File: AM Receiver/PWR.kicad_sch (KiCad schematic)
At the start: 10 parts, among them IC105 L78L08_SO8, IC106 L78L05_SO8, J100 Barrel_Jack_Switch

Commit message: Filled out information in User.Drawings on PCB
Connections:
- net +12V ...+15V renamed VIN
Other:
- note added: "Design Notes - Versorgung Eingang über J100: +12V ... +15V gegen GND. IC106 (L78L05) erzeugt +5V für PLL/Digitalteil; IC105 (L78L08) erzeugt +8V für RF/ZF-Analogteil. 78Lxx Regler sind für ca. 100 mA ausgelegt; Strombudget je Schiene darunter halten. Dropout/Verlustleistung: 12V Minimum gibt genuegend Reserve für 5V/8V Linearregler. C125/C130/C133 = 100 nF dienen als lokale Ein-/Ausgangsabblockun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"
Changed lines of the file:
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@@
 		(comment 3 "T. Brown")
+	)
+	(text "Design Notes - Versorgung\nEingang über J100: +12V ... +15V gegen GND.\nIC106 (L78L05) erzeugt +5V für PLL/Digitalteil; IC105 (L78L08) erzeugt +8V für RF/ZF-Analogteil.\n78Lxx Regler sind für ca. 100 mA ausgelegt; Strombudget je Schiene darunter halten.\nDropout/Verlustleistung: 12V Minimum gibt genuegend Reserve für 5V/8V Linearregler.\nC125/C130/C133 = 100 nF dienen als lokale Ein-/Ausgangsabblockung der Regler.\nTP_VIN, TP_5V, TP_8V und TP_GND sind Bring-up Messpunkte.\nTrennung +5V digital und +8V analog reduziert digitale Störung im RF/ZF-Teil."
+		(exclude_from_sim no)
+		(at 35.56 34.29 0)
+		(effects
+			(font
+				(size 1.27 1.27)
+			)
+			(justify left)
+		)
 	)
 	(junction
@@
 			)
 		)
-		(property "Value" "+12V ...+15V"
+		(property "Value" "VIN"
 			(at 107.696 88.9 0)
 			(show_name no)
@@
 			)
 		)
-		(property "Value" "+12V ...+15V"
+		(property "Value" "VIN"
 			(at 167.386 80.518 0)
 			(show_name no)
@@
 			)
 		)
-		(property "Value" "+12V ...+15V"
+		(property "Value" "VIN"
 			(at 214.376 80.518 0)
 			(show_name no)

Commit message: Updated Design notes in schematic
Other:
- note added: "Design Notes - Versorgung Eingang ueber J100: VIN, vorgesehen fuer 12V ... 15V gegen GND. IC106 (L78L05) erzeugt +5V fuer PLL/Digitalteil; IC105 (L78L08) erzeugt +8V fuer RF/ZF-Analogteil. 78Lxx Regler sind fuer ca. 100 mA ausgelegt; Strombudget je Schiene darunter halten. Dropout/Verlustleistung: 12V Minimum gibt genuegend Reserve fuer 5V/8V Linearregler. C125/C130/C133 = 100 nF dienen als lokal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"
- note removed: "Design Notes - Versorgung Eingang über J100: +12V ... +15V gegen GND. IC106 (L78L05) erzeugt +5V für PLL/Digitalteil; IC105 (L78L08) erzeugt +8V für RF/ZF-Analogteil. 78Lxx Regler sind für ca. 100 mA ausgelegt; Strombudget je Schiene darunter halten. Dropout/Verlustleistung: 12V Minimum gibt genuegend Reserve für 5V/8V Linearregler. C125/C130/C133 = 100 nF dienen als lokale Ein-/Ausgangsabblockun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"
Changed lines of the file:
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@@
 		(comment 3 "T. Brown")
 	)
-	(text "Design Notes - Versorgung\nEingang über J100: +12V ... +15V gegen GND.\nIC106 (L78L05) erzeugt +5V für PLL/Digitalteil; IC105 (L78L08) erzeugt +8V für RF/ZF-Analogteil.\n78Lxx Regler sind für ca. 100 mA ausgelegt; Strombudget je Schiene darunter halten.\nDropout/Verlustleistung: 12V Minimum gibt genuegend Reserve für 5V/8V Linearregler.\nC125/C130/C133 = 100 nF dienen als lokale Ein-/Ausgangsabblockung der Regler.\nTP_VIN, TP_5V, TP_8V und TP_GND sind Bring-up Messpunkte.\nTrennung +5V digital und +8V analog reduziert digitale Störung im RF/ZF-Teil."
+	(text "Design Notes - Versorgung\nEingang ueber J100: VIN, vorgesehen fuer 12V ... 15V gegen GND.\nIC106 (L78L05) erzeugt +5V fuer PLL/Digitalteil; IC105 (L78L08) erzeugt +8V fuer RF/ZF-Analogteil.\n78Lxx Regler sind fuer ca. 100 mA ausgelegt; Strombudget je Schiene darunter halten.\nDropout/Verlustleistung: 12V Minimum gibt genuegend Reserve fuer 5V/8V Linearregler.\nC125/C130/C133 = 100 nF dienen als lokale Ein-/Ausgangsabblockung der Regler.\nTP_VIN, TP_5V, TP_8V und TP_GND sind Bring-up Messpunkte.\nTrennung +5V digital und +8V analog reduziert digitale Stoerung im RF/ZF-Teil."
 		(exclude_from_sim no)
 		(at 35.56 34.29 0)

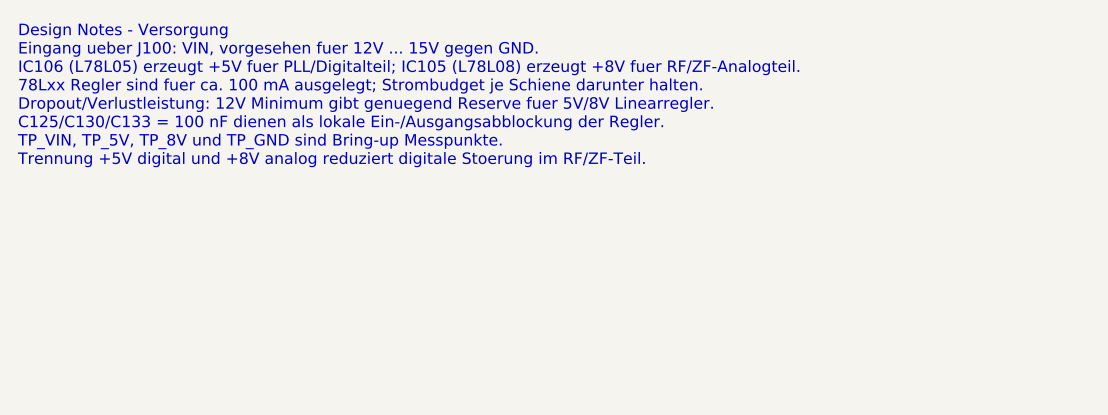
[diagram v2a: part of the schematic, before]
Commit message: updated schematic root page voltage
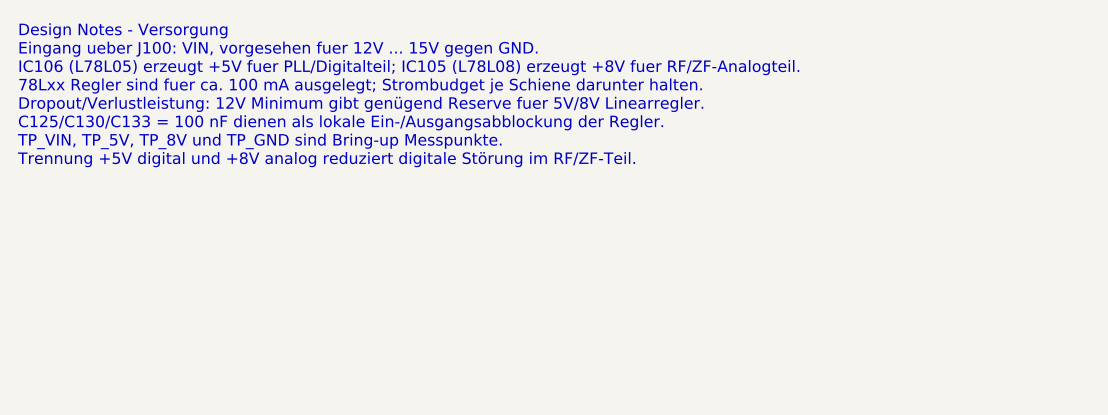
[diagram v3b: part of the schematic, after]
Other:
- note added: "Design Notes - Versorgung Eingang ueber J100: VIN, vorgesehen fuer 12V ... 15V gegen GND. IC106 (L78L05) erzeugt +5V fuer PLL/Digitalteil; IC105 (L78L08) erzeugt +8V fuer RF/ZF-Analogteil. 78Lxx Regler sind fuer ca. 100 mA ausgelegt; Strombudget je Schiene darunter halten. Dropout/Verlustleistung: 12V Minimum gibt genügend Reserve fuer 5V/8V Linearregler. C125/C130/C133 = 100 nF dienen als lokale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"
- note removed: "Design Notes - Versorgung Eingang ueber J100: VIN, vorgesehen fuer 12V ... 15V gegen GND. IC106 (L78L05) erzeugt +5V fuer PLL/Digitalteil; IC105 (L78L08) erzeugt +8V fuer RF/ZF-Analogteil. 78Lxx Regler sind fuer ca. 100 mA ausgelegt; Strombudget je Schiene darunter halten. Dropout/Verlustleistung: 12V Minimum gibt genuegend Reserve fuer 5V/8V Linearregler. C125/C130/C133 = 100 nF dienen als lokal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"
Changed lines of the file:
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@@
 		(comment 3 "T. Brown")
 	)
-	(text "Design Notes - Versorgung\nEingang ueber J100: VIN, vorgesehen fuer 12V ... 15V gegen GND.\nIC106 (L78L05) erzeugt +5V fuer PLL/Digitalteil; IC105 (L78L08) erzeugt +8V fuer RF/ZF-Analogteil.\n78Lxx Regler sind fuer ca. 100 mA ausgelegt; Strombudget je Schiene darunter halten.\nDropout/Verlustleistung: 12V Minimum gibt genuegend Reserve fuer 5V/8V Linearregler.\nC125/C130/C133 = 100 nF dienen als lokale Ein-/Ausgangsabblockung der Regler.\nTP_VIN, TP_5V, TP_8V und TP_GND sind Bring-up Messpunkte.\nTrennung +5V digital und +8V analog reduziert digitale Stoerung im RF/ZF-Teil."
+	(text "Design Notes - Versorgung\nEingang ueber J100: VIN, vorgesehen fuer 12V ... 15V gegen GND.\nIC106 (L78L05) erzeugt +5V fuer PLL/Digitalteil; IC105 (L78L08) erzeugt +8V fuer RF/ZF-Analogteil.\n78Lxx Regler sind fuer ca. 100 mA ausgelegt; Strombudget je Schiene darunter halten.\nDropout/Verlustleistung: 12V Minimum gibt genügend Reserve fuer 5V/8V Linearregler.\nC125/C130/C133 = 100 nF dienen als lokale Ein-/Ausgangsabblockung der Regler.\nTP_VIN, TP_5V, TP_8V und TP_GND sind Bring-up Messpunkte.\nTrennung +5V digital und +8V analog reduziert digitale Störung im RF/ZF-Teil."
 		(exclude_from_sim no)
 		(at 35.56 34.29 0)

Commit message: Updated Deckblatt
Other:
- note added: "Design Notes - Versorgung Eingang ueber J100: VIN, vorgesehen fuer 12V ... 15V gegen GND. IC106 (L78L05) erzeugt +5V fuer PLL/Digitalteil; IC105 (L78L08) erzeugt +8V für RF/ZF-Analogteil. 78Lxx Regler sind für ca. 100 mA ausgelegt; Strombudget je Schiene darunter halten. Dropout/Verlustleistung: 12V Minimum gibt genügend Reserve für 5V/8V Linearregler. C125/C130/C133 = 100 nF dienen als lokale Ei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"
- note removed: "Design Notes - Versorgung Eingang ueber J100: VIN, vorgesehen fuer 12V ... 15V gegen GND. IC106 (L78L05) erzeugt +5V fuer PLL/Digitalteil; IC105 (L78L08) erzeugt +8V fuer RF/ZF-Analogteil. 78Lxx Regler sind fuer ca. 100 mA ausgelegt; Strombudget je Schiene darunter halten. Dropout/Verlustleistung: 12V Minimum gibt genügend Reserve fuer 5V/8V Linearregler. C125/C130/C133 = 100 nF dienen als lokale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"
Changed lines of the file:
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@@
 		(comment 3 "T. Brown")
 	)
-	(text "Design Notes - Versorgung\nEingang ueber J100: VIN, vorgesehen fuer 12V ... 15V gegen GND.\nIC106 (L78L05) erzeugt +5V fuer PLL/Digitalteil; IC105 (L78L08) erzeugt +8V fuer RF/ZF-Analogteil.\n78Lxx Regler sind fuer ca. 100 mA ausgelegt; Strombudget je Schiene darunter halten.\nDropout/Verlustleistung: 12V Minimum gibt genügend Reserve fuer 5V/8V Linearregler.\nC125/C130/C133 = 100 nF dienen als lokale Ein-/Ausgangsabblockung der Regler.\nTP_VIN, TP_5V, TP_8V und TP_GND sind Bring-up Messpunkte.\nTrennung +5V digital und +8V analog reduziert digitale Störung im RF/ZF-Teil."
+	(text "Design Notes - Versorgung\nEingang ueber J100: VIN, vorgesehen fuer 12V ... 15V gegen GND.\nIC106 (L78L05) erzeugt +5V fuer PLL/Digitalteil; IC105 (L78L08) erzeugt +8V für RF/ZF-Analogteil.\n78Lxx Regler sind für ca. 100 mA ausgelegt; Strombudget je Schiene darunter halten.\nDropout/Verlustleistung: 12V Minimum gibt genügend Reserve für 5V/8V Linearregler.\nC125/C130/C133 = 100 nF dienen als lokale Ein-/Ausgangsabblockung der Regler.\nTP_VIN, TP_5V, TP_8V und TP_GND sind Bring-up Messpunkte.\nTrennung +5V digital und +8V analog reduziert digitale Störung im RF/ZF-Teil."
 		(exclude_from_sim no)
 		(at 35.56 34.29 0)
